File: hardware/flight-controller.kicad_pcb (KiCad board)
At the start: 4 copper layers, 70 x 70 mm, 121 parts, among them J1 USB_C_Receptacle_USB2.0_16P, J10 Screw_Terminal_01x02, J11 Micro_SD_Card_Det_Hirose_DM3AT, J12 Conn_01x03, J13 Conn_01x03, J14 Conn_01x03, J15 Conn_01x03, J16 Screw_Terminal_01x02, J17 Conn_01x04, J18 Screw_Terminal_01x02, J19 Conn_01x02, J2 Conn_01x02, J20 Conn_01x02, J21 Conn_01x02, J22 Conn_01x02, J23 Conn_01x02, J3 Conn_Coaxial, J4 Conn_01x04, J5 Screw_Terminal_01x02, J6 Conn_01x04, J7 Screw_Terminal_01x02, J8 Conn_01x04, J9 Screw_Terminal_01x02, U1 BMP384, U2 LSM6DSOTR, U3 MMC5983MA, U4 NEO-M9N, U5 TPS2121RUXR, U6 AP62300TWU, U7 STM32H723VGTx, Y1 Q13FC13500004, Y2 X322525MOB4SI

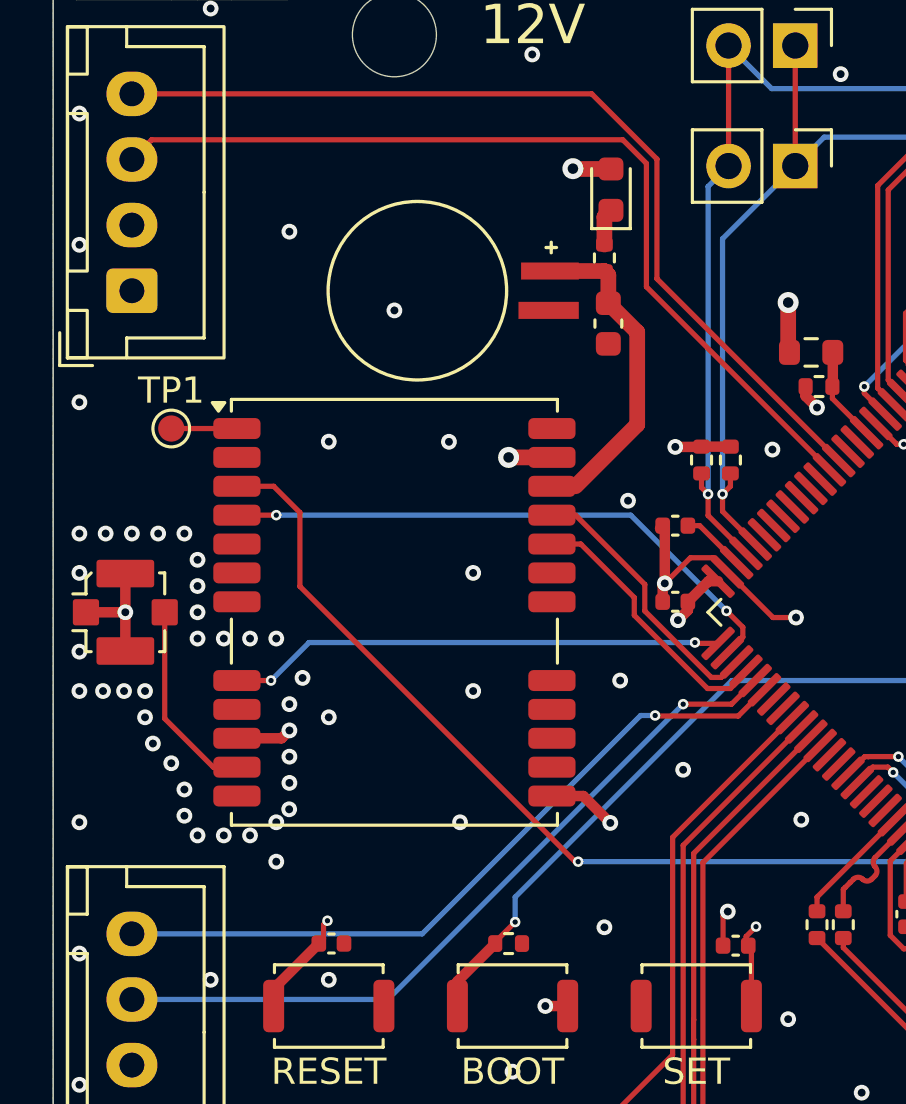
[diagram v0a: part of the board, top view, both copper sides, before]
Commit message: replaced gps with max-m10s
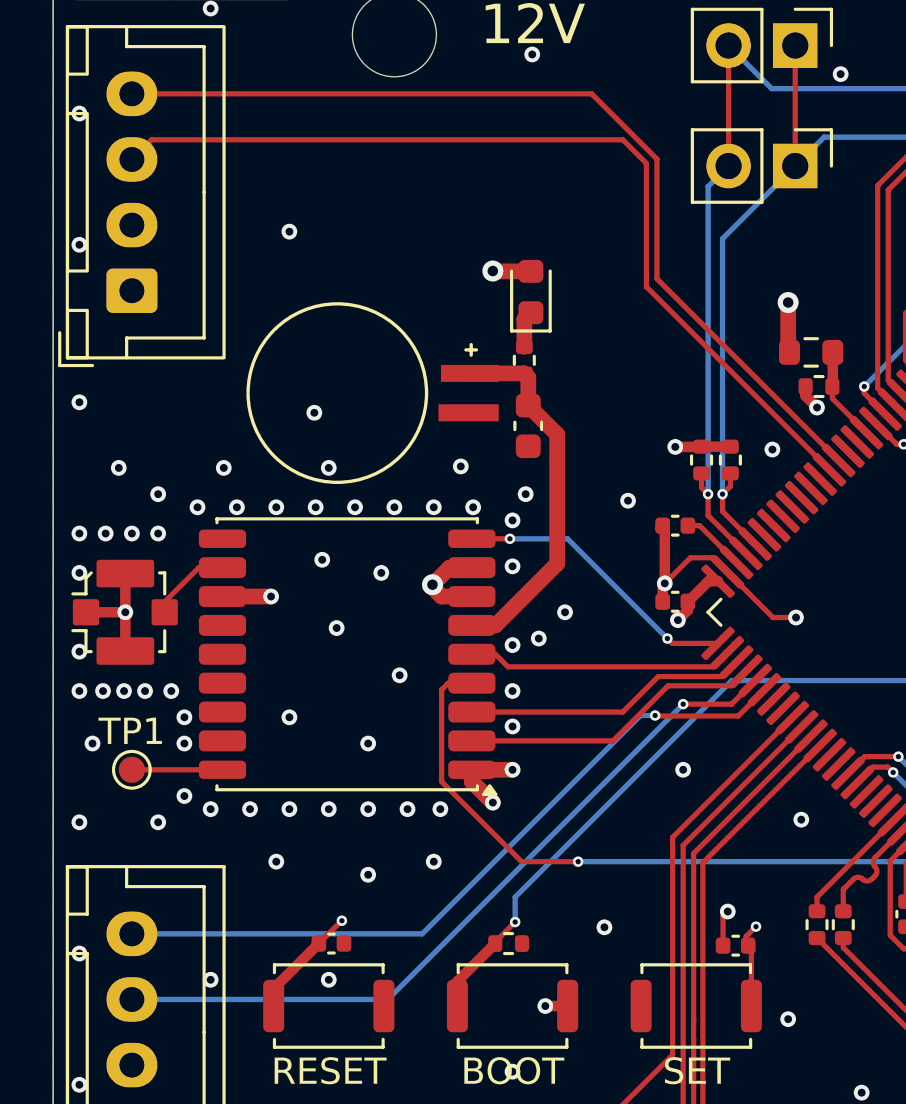
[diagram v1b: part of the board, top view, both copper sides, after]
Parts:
- removed U4: NEO-M9N, RF_GPS:ublox_NEO
- added U8: MAX-M10S, RF_GPS:ublox_MAX, F.Cu at (118.2, 104.6)
- moved TP1 13.1 mm to (110.0, 109.0)
- moved C8 4.95 mm to (125.1, 95.9)
- moved BT1 4.95 mm to (117.8, 94.7)
- moved R3 4.95 mm to (125.0, 93.4)
- moved D1 4.95 mm to (125.2, 90.8)
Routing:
- net /GPS_INT: track 22.3 -> 10.2 mm, vias 2 -> 0
- net /GPS_LED: track 68.5 -> 59.2 mm
- net /GPS_RESET: track 18.9 -> 11.0 mm
- net Net-(J3-In): track 7.57 -> 3.14 mm
- net /V_BCKP: track 11.8 -> 14.1 mm
- net +3.3V: track 87.0 -> 88.9 mm
- net /GPS_RX: track 10.2 -> 11.5 mm
- net /RESET: track 41.1 -> 40.0 mm
- net Net-(U8-~{SAFEBOOT}): track 2.50 -> 3.45 mm
- net GND: track 98.2 -> 98.4 mm, vias 184 -> 198

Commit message: touching up pcb
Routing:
- net /UART7_TX: track 34.8 -> 32.9 mm
- net /GPS_LED: track 59.2 -> 58.3 mm
- net GND: track 98.4 -> 99.1 mm, vias 198 -> 201
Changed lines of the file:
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@@
 	)
 	(segment
+		(start 133.810913 102.589087)
+		(end 132.683868 101.462043)
+		(width 0.2)
+		(layer "F.Cu")
+		(net 3)
+	)
+	(segment
 		(start 152.135 131.94)
 		(end 152.135 132.365)
@@
 	)
 	(segment
-		(start 134.421825 103.2)
-		(end 135.3 103.2)
-		(width 0.2)
-		(layer "F.Cu")
-		(net 3)
-	)
-	(segment
 		(start 115.3 102.4)
 		(end 113.45 102.4)
@@
 	)
 	(segment
+		(start 161.775 105.725)
+		(end 161.8 105.7)
+		(width 0.4)
+		(layer "F.Cu")
+		(net 3)
+	)
+	(segment
 		(start 140.44 88.94)
 		(end 141.4 89.9)
@@
 	)
 	(segment
+		(start 151.2 96.4)
+		(end 150.7 96.9)
+		(width 0.4)
+		(layer "F.Cu")
+		(net 3)
+	)
+	(segment
 		(start 146.812034 94.912034)
 		(end 147.4 95.5)
@@
 	)
 	(segment
-		(start 146.6 100.521321)
-		(end 146.6 100.6)
-		(width 0.2)
+		(start 154.8 95.3)
+		(end 154.796188 95.296188)
+		(width 0.4)
 		(layer "F.Cu")
 		(net 3)
 	)
 	(segment
-		(start 154.8 95.3)
-		(end 154.796188 95.296188)
-		(width 0.4)
+		(start 142.5 110.278175)
+		(end 140.462043 112.316132)
+		(width 0.2)
 		(layer "F.Cu")
 		(net 3)
@@
 	)
 	(segment
-		(start 150.7 96.9)
-		(end 151.2 96.4)
-		(width 0.4)
-		(layer "F.Cu")
-		(net 3)
-	)
-	(segment
 		(start 149.85 94.55)
 		(end 149.85 93.6)
@@
 	)
 	(segment
+		(start 160.175 105.725)
+		(end 161.775 105.725)
+		(width 0.4)
+		(layer "F.Cu")
+		(net 3)
+	)
+	(segment
 		(start 149.85 130.75)
 		(end 149.85 130.9)
@@
 	)
 	(segment
+		(start 150.7 96.9)
+		(end 150.68 96.9)
+		(width 0.4)
+		(layer "F.Cu")
+		(net 3)
+	)
+	(segment
 		(start 155.275 102.525)
 		(end 155.2 102.6)
@@
 	)
 	(segment
-		(start 142.5 110.278175)
-		(end 142.5 110)
-		(width 0.2)
-		(layer "F.Cu")
-		(net 3)
-	)
-	(segment
 		(start 142.52 87.364326)
 		(end 142.076 86.920326)
@@
 	)
 	(segment
-		(start 132.683868 101.462043)
-		(end 134.421825 103.2)
-		(width 0.2)
-		(layer "F.Cu")
-		(net 3)
-	)
-	(segment
 		(start 140.815596 93.330315)
 		(end 141.319628 93.330315)
@@
 	)
 	(segment
+		(start 161.575 98.675)
+		(end 161.6 98.7)
+		(width 0.4)
+		(layer "F.Cu")
+		(net 3)
+	)
+	(segment
 		(start 142.52 88.1)
 		(end 142.449 88.029)
@@
 	)
 	(segment
-		(start 148.3 103.9)
+		(start 148.7 103.9)
 		(end 150.678175 103.9)
 		(width 0.2)
@@
 	)
 	(segment
-		(start 150.678175 103.9)
-		(end 151.316132 104.537957)
-		(width 0.2)
-		(layer "F.Cu")
-		(net 3)
-	)
-	(segment
 		(start 158.95 131.75)
 		(end 158.95 132.55)
@@
 	)
 	(segment
+		(start 146.578679 100.521321)
+		(end 146.6 100.521321)
+		(width 0.2)
+		(layer "F.Cu")
+		(net 3)
+	)
+	(segment
 		(start 148.4 91.42)
 		(end 148.4 90.7)
@@
 	)
 	(segment
-		(start 140.462043 112.316132)
-		(end 142.5 110.278175)
-		(width 0.2)
+		(start 160.175 98.675)
+		(end 161.575 98.675)
+		(width 0.4)
 		(layer "F.Cu")
 		(net 3)
@@
 	)
 	(segment
+		(start 146.6 100.521321)
+		(end 148.487705 98.633616)
+		(width 0.2)
+		(layer "F.Cu")
+		(net 3)
+	)
+	(segment
+		(start 146.5 100.6)
+		(end 146.578679 100.521321)
+		(width 0.2)
+		(layer "F.Cu")
+		(net 3)
+	)
+	(segment
 		(start 141.6 85.8)
 		(end 142 86.2)
@@
 	)
 	(segment
-		(start 148.487705 98.633616)
-		(end 146.6 100.521321)
-		(width 0.2)
-		(layer "F.Cu")
-		(net 3)
-	)
-	(segment
 		(start 143.757359 97)
 		(end 145.305724 95.451635)
@@
 	)
 	(segment
+		(start 150.678175 103.9)
+		(end 151.316132 104.537957)
+		(width 0.2)
+		(layer "F.Cu")
+		(net 3)
+	)
+	(segment
 		(start 154.48 104)
 		(end 154.48 103.32)
@@
 	)
 	(segment
-		(start 150.68 96.9)
-		(end 150.7 96.9)
-		(width 0.4)
-		(layer "F.Cu")
-		(net 3)
-	)
-	(segment
 		(start 143.361091 97.038909)
 		(end 143.4 97)
@@
 	)
 	(via
-		(at 135.3 103.2)
+		(at 133.810913 102.589087)
 		(size 0.6)
 		(drill 0.3)
@@
 	)
 	(via
-		(at 148.3 103.9)
+		(at 148.7 103.9)
 		(size 0.6)
 		(drill 0.3)
@@
 	)
 	(via
+		(at 115.7 84.5)
+		(size 0.6)
+		(drill 0.3)
+		(layers "F.Cu" "B.Cu")
+		(free yes)
+		(net 3)
+	)
+	(via
 		(at 176 79)
 		(size 0.6)
@@
 	)
 	(via
-		(at 146.6 100.6)
+		(at 146.5 100.6)
 		(size 0.6)
 		(drill 0.3)
@@
 	)
 	(via
-		(at 142.5 110)
+		(at 142.5 110.278175)
+		(size 0.6)
+		(drill 0.3)
+		(layers "F.Cu" "B.Cu")
+		(free yes)
+		(net 3)
+	)
+	(via
+		(at 161.6 98.7)
 		(size 0.6)
 		(drill 0.3)
@@
 	)
 	(via
+		(at 124.6 84.5)
+		(size 0.6)
+		(drill 0.3)
+		(layers "F.Cu" "B.Cu")
+		(free yes)
+		(net 3)
+	)
+	(via
 		(at 109.7 106)
 		(size 0.6)
@@
 	)
 	(via
-		(at 116 88.5)
+		(at 119.7 88.8)
 		(size 0.6)
 		(drill 0.3)
@@
 	)
 	(via
-		(at 164 105)
+		(at 161.8 105.7)
 		(size 0.6)
 		(drill 0.3)
@@
 	)
 	(segment
-		(start 163 130.7)
-		(end 163 129.2)
+		(start 165.4875 133.1875)
+		(end 165.5 133.1875)
 		(width 0.2)
 		(layer "F.Cu")
@@
 	)
 	(segment
-		(start 165.4875 133.1875)
-		(end 163 130.7)
+		(start 164.65 132.35)
+		(end 165.4875 133.1875)
 		(width 0.2)
 		(layer "F.Cu")
@@
 		(net 60)
 	)
-	(segment
-		(start 165.5 133.1875)
-		(end 165.4875 133.1875)
-		(width 0.2)
-		(layer "F.Cu")
-		(net 60)
-	)
 	(via
 		(at 127 112.5)
@@
 	)
 	(via
-		(at 163 129.2)
+		(at 164.65 132.35)
 		(size 0.4)
 		(drill 0.2)
@@
 	)
 	(segment
-		(start 156.3 129.2)
-		(end 139.6 112.5)
+		(start 139.6 112.5)
+		(end 127 112.5)
 		(width 0.2)
 		(layer "B.Cu")
@@
 	)
 	(segment
-		(start 163 129.2)
+		(start 164.65 132.35)
+		(end 161.5 129.2)
+		(width 0.2)
+		(layer "B.Cu")
+		(net 60)
+	)
+	(segment
+		(start 161.5 129.2)
 		(end 156.3 129.2)
 		(width 0.2)
@@
 	)
 	(segment
-		(start 139.6 112.5)
-		(end 127 112.5)
+		(start 156.3 129.2)
+		(end 139.6 112.5)
 		(width 0.2)
 		(layer "B.Cu")
@@
 	)
 	(segment
-		(start 129.6 90.6)
-		(end 136.572955 97.572955)
+		(start 110.05 85.7)
+		(end 127.1 85.7)
 		(width 0.2)
 		(layer "F.Cu")
@@
 	)
 	(segment
-		(start 110 85.75)
-		(end 110.75 85)
+		(start 129.5 90.5)
+		(end 136.572955 97.572955)
 		(width 0.2)
 		(layer "F.Cu")
@@
 	)
 	(segment
-		(start 129.6 85.9)
-		(end 129.6 90.6)
+		(start 127.1 85.7)
+		(end 129.5 88.1)
 		(width 0.2)
 		(layer "F.Cu")
@@
 	)
 	(segment
-		(start 110.75 85)
-		(end 128.7 85)
+		(start 129.5 88.1)
+		(end 129.5 90.5)
 		(width 0.2)
 		(layer "F.Cu")
@@
 	)
 	(segment
-		(start 128.7 85)
-		(end 129.6 85.9)
+		(start 110 85.75)
+		(end 110.05 85.7)
 		(width 0.2)
 		(layer "F.Cu")

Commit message: added silkscreen
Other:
- board text added: "Fly you fools!"
- board text added: "v1.0"
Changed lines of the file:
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@@
+		)
+	)
+	(gr_text "v1.0"
+		(at 148 136.5 0)
+		(layer "F.SilkS")
+		(effects
+			(font
+				(size 1.3 1.3)
+				(thickness 0.1625)
+			)
+			(justify left bottom)
 		)
 	)
@@
 		)
 	)
+	(gr_text "Fly you fools!"
+		(at 159 137.37 -0)
+		(layer "B.SilkS")
+		(effects
+			(font
+				(size 1 1)
+				(thickness 0.1)
+			)
+			(justify left bottom mirror)
+		)
+	)
